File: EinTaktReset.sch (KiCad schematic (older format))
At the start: 22 parts

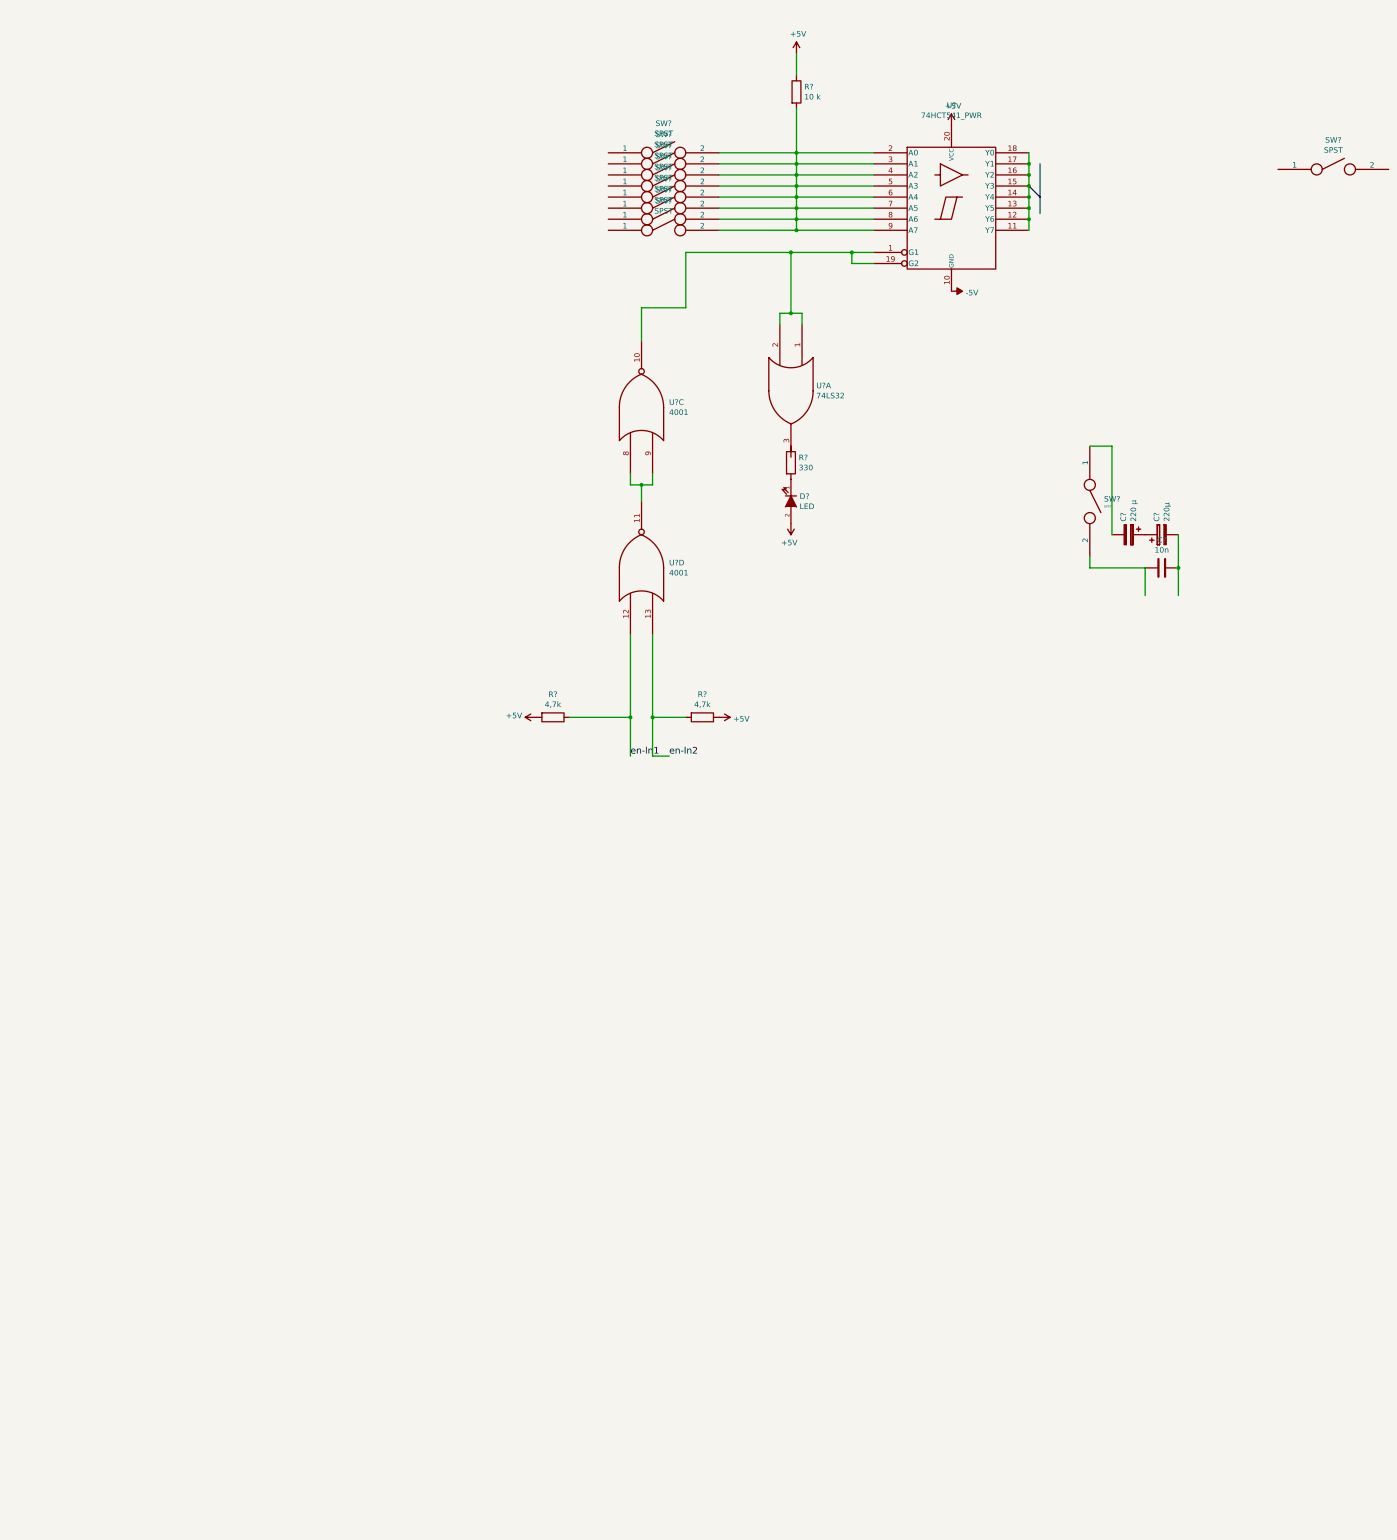
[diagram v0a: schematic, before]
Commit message: Schaltplan weitergeführt
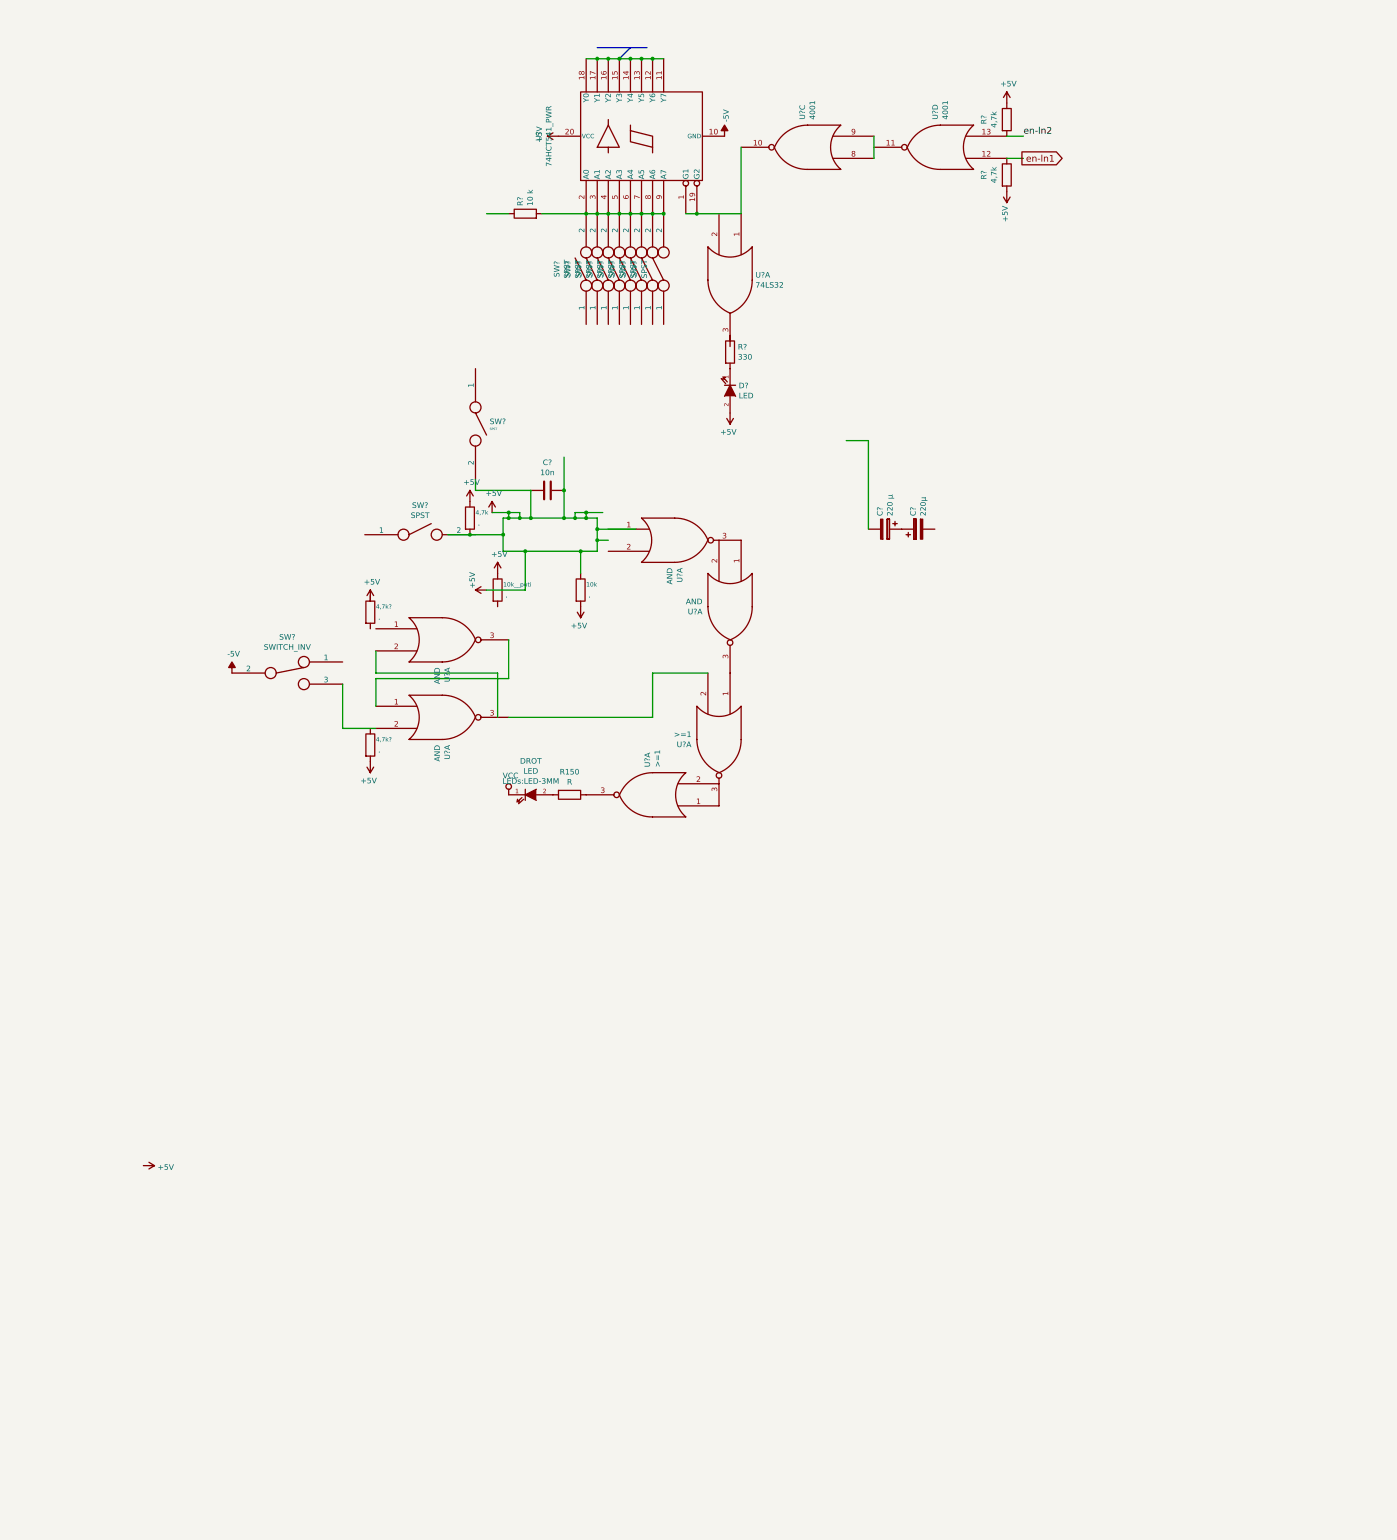
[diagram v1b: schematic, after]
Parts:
- removed SW?: SPST, symbol SPST
- added 10k, 10k__poti, 4,7k, 4,7k? (x2): ., symbol R
- added DROT: LED, LEDs:LED-3MM, symbol LED
- added R150: R, symbol R
- added SW?: SPST, symbol SPST
- added SW?: SWITCH_INV, symbol SWITCH_INV
- added U? (x4): AND, symbol 4001
- added U? (x2): >=1, symbol 4001
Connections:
- net labels added: VCC
- wire segments 36 -> 41
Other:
- moved on the sheet: C?, D?, R?, SW?, U?, U?A, U?C, U?D

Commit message: added lib
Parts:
- added IC?: 74LS624, symbol 74LS624
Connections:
- wire segments 41 -> 37
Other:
- moved on the sheet: 10k, 10k__poti, 4,7k, C?, SW?
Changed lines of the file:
@@
 LIBS:contrib
 LIBS:valves
+LIBS:vco
 LIBS:EinTaktReset-cache
 EELAYER 25 0
@@
 	0    1    1    0
 $EndComp
-Wire Wire Line
-	3100 5050 3100 4500
 $Comp
 L C C?
 U 1 1 57E97853
-P 2950 4800
-F 0 "C?" V 2698 4800 50  0000 C CNN
-F 1 "10n" V 2789 4800 50  0000 C CNN
-F 2 "" H 2988 4650 50  0000 C CNN
-F 3 "" H 2950 4800 50  0000 C CNN
-	1    2950 4800
-	0    1    1    0
-$EndComp
-Wire Wire Line
-	2800 4800 2300 4800
-Wire Wire Line
-	2300 4800 2300 4700
-Connection ~ 3100 4800
-Wire Wire Line
-	2800 5050 2800 4800
+P 2850 4100
+F 0 "C?" V 2598 4100 50  0000 C CNN
+F 1 "10n" V 2689 4100 50  0000 C CNN
+F 2 "" H 2888 3950 50  0000 C CNN
+F 3 "" H 2850 4100 50  0000 C CNN
+	1    2850 4100
+	0    1    1    0
+$EndComp
+Wire Wire Line
+	2200 4100 2200 4000
 $Comp
 L SPST SW?
 U 1 1 57E97A95
-P 2300 4200
-F 0 "SW?" V 2278 4328 50  0000 L CNN
-F 1 "SPST" V 2345 4328 20  0000 L CNN
-F 2 "" H 2300 4200 50  0000 C CNN
-F 3 "" H 2300 4200 50  0000 C CNN
-	1    2300 4200
+P 2200 3500
+F 0 "SW?" V 2178 3628 50  0000 L CNN
+F 1 "SPST" V 2245 3628 20  0000 L CNN
+F 2 "" H 2200 3500 50  0000 C CNN
+F 3 "" H 2200 3500 50  0000 C CNN
+	1    2200 3500
 	0    1    1    0
 $EndComp
@@
 	5850 4350 5850 5150
 Wire Wire Line
-	2550 5050 3400 5050
-Wire Wire Line
-	3400 5050 3400 5350
-Connection ~ 3100 5050
-Wire Wire Line
-	3400 5350 2550 5350
-Wire Wire Line
-	2550 5350 2550 5050
-Connection ~ 2800 5050
-Wire Wire Line
-	2700 5000 2700 5050
-Wire Wire Line
-	2450 5000 2700 5000
-Connection ~ 2700 5050
-Wire Wire Line
-	2600 5050 2600 5000
-Connection ~ 2600 5000
-Connection ~ 2600 5050
-Wire Wire Line
-	3200 5050 3200 5000
-Wire Wire Line
-	3200 5000 3450 5000
-Connection ~ 3200 5050
-Wire Wire Line
-	3300 5000 3300 5050
-Connection ~ 3300 5050
-Connection ~ 3300 5000
-Wire Wire Line
-	3400 5150 3750 5150
-Connection ~ 3400 5150
-Wire Wire Line
-	3400 5250 3500 5250
-Connection ~ 3400 5250
-Wire Wire Line
-	3250 5350 3250 5550
-Connection ~ 3250 5350
-Wire Wire Line
-	2750 5350 2750 5700
-Connection ~ 2750 5350
-Wire Wire Line
-	2050 5200 2550 5200
-Connection ~ 2550 5200
+	2300 4600 2550 4600
+Wire Wire Line
+	1350 5100 2050 5100
 $Comp
 L R 4,7k
 U 1 1 5845B97A
-P 2250 5050
-F 0 "4,7k" H 2300 5100 39  0000 L CNN
-F 1 "." H 2320 5005 50  0000 L CNN
-F 2 "" V 2180 5050 50  0000 C CNN
-F 3 "" H 2250 5050 50  0000 C CNN
-	1    2250 5050
-	1    0    0    -1
-$EndComp
-Connection ~ 2250 5200
+P 1550 4950
+F 0 "4,7k" H 1600 5000 39  0000 L CNN
+F 1 "." H 1620 4905 50  0000 L CNN
+F 2 "" V 1480 4950 50  0000 C CNN
+F 3 "" H 1550 4950 50  0000 C CNN
+	1    1550 4950
+	1    0    0    -1
+$EndComp
+Connection ~ 1550 5100
 $Comp
 L SPST SW?
 U 1 1 5845BEEF
-P 1800 5200
-F 0 "SW?" H 1800 5465 50  0000 C CNN
-F 1 "SPST" H 1800 5374 50  0000 C CNN
-F 2 "" H 1800 5200 50  0000 C CNN
-F 3 "" H 1800 5200 50  0000 C CNN
-	1    1800 5200
+P 1100 5100
+F 0 "SW?" H 1100 5365 50  0000 C CNN
+F 1 "SPST" H 1100 5274 50  0000 C CNN
+F 2 "" H 1100 5100 50  0000 C CNN
+F 3 "" H 1100 5100 50  0000 C CNN
+	1    1100 5100
 	1    0    0    -1
 $EndComp
@@
 L R 10k
 U 1 1 5845CFFB
-P 3250 5700
-F 0 "10k" H 3300 5750 39  0000 L CNN
-F 1 "." H 3320 5655 50  0000 L CNN
-F 2 "" V 3180 5700 50  0000 C CNN
-F 3 "" H 3250 5700 50  0000 C CNN
-	1    3250 5700
+P 2900 5850
+F 0 "10k" H 2950 5900 39  0000 L CNN
+F 1 "." H 2970 5805 50  0000 L CNN
+F 2 "" V 2830 5850 50  0000 C CNN
+F 3 "" H 2900 5850 50  0000 C CNN
+	1    2900 5850
 	1    0    0    -1
 $EndComp
@@
 L R 10k__poti
 U 1 1 5845D124
-P 2500 5700
-F 0 "10k__poti" H 2550 5750 39  0000 L CNN
-F 1 "." H 2570 5655 50  0000 L CNN
-F 2 "" V 2430 5700 50  0000 C CNN
-F 3 "" H 2500 5700 50  0000 C CNN
-	1    2500 5700
-	1    0    0    -1
-$EndComp
-Wire Wire Line
-	2750 5700 2400 5700
+P 2200 5700
+F 0 "10k__poti" H 2250 5750 39  0000 L CNN
+F 1 "." H 2270 5655 50  0000 L CNN
+F 2 "" V 2130 5700 50  0000 C CNN
+F 3 "" H 2200 5700 50  0000 C CNN
+	1    2200 5700
+	1    0    0    -1
+$EndComp
+Wire Wire Line
+	2450 5700 2100 5700
 $Comp
 L +5V #PWR?
 U 1 1 5845D52B
-P 2400 5700
-F 0 "#PWR?" H 2400 5550 50  0001 C CNN
-F 1 "+5V" H 2415 5828 0   0000 L CNN
-F 2 "" H 2400 5700 50  0000 C CNN
-F 3 "" H 2400 5700 50  0000 C CNN
-	1    2400 5700
+P 2100 5700
+F 0 "#PWR?" H 2100 5550 50  0001 C CNN
+F 1 "+5V" H 2115 5828 60  0000 L CNN
+F 2 "" H 2100 5700 50  0000 C CNN
+F 3 "" H 2100 5700 50  0000 C CNN
+	1    2100 5700
 	0    -1   -1   0
 $EndComp
@@
 L +5V #PWR?
 U 1 1 5845DB56
-P 2500 5550
-F 0 "#PWR?" H 2500 5400 50  0001 C CNN
-F 1 "+5V" H 2515 5723 50  0000 C CNN
-F 2 "" H 2500 5550 50  0000 C CNN
-F 3 "" H 2500 5550 50  0000 C CNN
-	1    2500 5550
+P 2200 5550
+F 0 "#PWR?" H 2200 5400 50  0001 C CNN
+F 1 "+5V" H 2215 5723 50  0000 C CNN
+F 2 "" H 2200 5550 50  0000 C CNN
+F 3 "" H 2200 5550 50  0000 C CNN
+	1    2200 5550
 	1    0    0    -1
 $EndComp
@@
 L +5V #PWR?
 U 1 1 5845DBA0
-P 2250 4900
-F 0 "#PWR?" H 2250 4750 50  0001 C CNN
-F 1 "+5V" H 2265 5073 50  0000 C CNN
-F 2 "" H 2250 4900 50  0000 C CNN
-F 3 "" H 2250 4900 50  0000 C CNN
-	1    2250 4900
+P 1550 4800
+F 0 "#PWR?" H 1550 4650 50  0001 C CNN
+F 1 "+5V" H 1565 4973 50  0000 C CNN
+F 2 "" H 1550 4800 50  0000 C CNN
+F 3 "" H 1550 4800 50  0000 C CNN
+	1    1550 4800
 	1    0    0    -1
 $EndComp
@@
 L +5V #PWR?
 U 1 1 5845DBEA
-P 2450 5000
-F 0 "#PWR?" H 2450 4850 50  0001 C CNN
-F 1 "+5V" H 2465 5173 50  0000 C CNN
-F 2 "" H 2450 5000 50  0000 C CNN
-F 3 "" H 2450 5000 50  0000 C CNN
-	1    2450 5000
+P 2300 4600
+F 0 "#PWR?" H 2300 4450 50  0001 C CNN
+F 1 "+5V" H 2315 4773 50  0000 C CNN
+F 2 "" H 2300 4600 50  0000 C CNN
+F 3 "" H 2300 4600 50  0000 C CNN
+	1    2300 4600
 	1    0    0    -1
 $EndComp
@@
 L +5V #PWR?
 U 1 1 5845DC34
-P 3250 5850
-F 0 "#PWR?" H 3250 5700 50  0001 C CNN
-F 1 "+5V" H 3265 6023 50  0000 C CNN
-F 2 "" H 3250 5850 50  0000 C CNN
-F 3 "" H 3250 5850 50  0000 C CNN
-	1    3250 5850
+P 2900 6000
+F 0 "#PWR?" H 2900 5850 50  0001 C CNN
+F 1 "+5V" H 2915 6173 50  0000 C CNN
+F 2 "" H 2900 6000 50  0000 C CNN
+F 3 "" H 2900 6000 50  0000 C CNN
+	1    2900 6000
 	-1   0    0    1
 $EndComp
@@
 Text GLabel 7600 1800 0    60   Input ~ 0
 en-ln1
+$Comp
+L 74LS624 IC?
+U 1 1 5A158E16
+P 2700 5100
+F 0 "IC?" H 2650 5200 60  0000 C CNN
+F 1 "74LS624" H 2700 5100 60  0000 C CNN
+F 2 "" H 2700 5100 60  0001 C CNN
+F 3 "" H 2700 5100 60  0001 C CNN
+	1    2700 5100
+	1    0    0    -1
+$EndComp
+Wire Wire Line
+	2700 4100 2700 4600
+Connection ~ 3000 4100
+Wire Wire Line
+	2700 4100 2200 4100
+Wire Wire Line
+	3000 4350 3000 3800
+Wire Wire Line
+	3000 4350 2800 4350
+Wire Wire Line
+	2800 4350 2800 4600
+Wire Wire Line
+	3350 4950 3450 4950
+Wire Wire Line
+	3450 4950 3450 5150
+Wire Wire Line
+	3450 5150 3500 5150
+Wire Wire Line
+	2900 4600 3200 4600
+Wire Wire Line
+	3200 4600 3200 4650
+Wire Wire Line
+	2450 5700 2450 5550
+Wire Wire Line
+	2900 5550 2900 5700
 $EndSCHEMATC

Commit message: .sch datei leicht verändert
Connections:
- net labels added: GND
- net labels removed: -5V
- wire segments 37 -> 43
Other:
- moved on the sheet: R?, SW?

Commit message: changes in eintaktreset .sch
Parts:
- added P? (x2): CONN_02X10, symbol CONN_02X10
- added U?: 74540, symbol 74540
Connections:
- wire segments 43 -> 46
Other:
- moved on the sheet: 10k, 10k__poti, 4,7k, 4,7k?, C?, D?, DROT, IC?, R150, R?, SW?, U?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

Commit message: changes in eintaktres .sch
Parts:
- added 10k? (x2): ., symbol R
- added C?: 10 µ, symbol CP
- added C?: 47µ, symbol CP
- added R?: 100, symbol R
- added SW?: SPST, symbol SPST
- added U? (x2): 74540, symbol 74540
- added U? (x2): AND, symbol 4001
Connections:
- wire segments 46 -> 67
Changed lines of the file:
@@
 	1    0    0    -1
-$EndComp
-$Comp
-L +5V #PWR?
-U 1 1 57E966CE
-P -650 11250
-F 0 "#PWR?" H -650 11100 50  0001 C CNN
-F 1 "+5V" V -635 11378 50  0000 L CNN
-F 2 "" H -650 11250 50  0000 C CNN
-F 3 "" H -650 11250 50  0000 C CNN
-	1    -650 11250
-	0    1    1    0
 $EndComp
 Text Label 7400 1950 0    60   ~ 0
@@
 	0    -1   -1   0
 $EndComp
+$Comp
+L 74540 U?
+U 1 1 5A31340A
+P 1450 9150
+F 0 "U?" H 1550 9250 60  0000 C CNN
+F 1 "74540" H 1600 9000 60  0000 C CNN
+F 2 "" H 1600 9000 60  0001 C CNN
+F 3 "" H 1600 9000 60  0001 C CNN
+	1    1450 9150
+	0    -1   -1   0
+$EndComp
+$Comp
+L 74540 U?
+U 1 1 5A313566
+P 1450 10000
+F 0 "U?" H 1550 10100 60  0000 C CNN
+F 1 "74540" H 1600 9850 60  0000 C CNN
+F 2 "" H 1600 9850 60  0001 C CNN
+F 3 "" H 1600 9850 60  0001 C CNN
+	1    1450 10000
+	0    -1   -1   0
+$EndComp
+Wire Wire Line
+	1450 9600 1450 9500
+Wire Wire Line
+	1450 8750 1450 8650
+Wire Wire Line
+	1450 10350 1450 10500
+Wire Wire Line
+	1450 10500 950  10500
+$Comp
+L R 10k?
+U 1 1 5A314363
+P 950 10300
+F 0 "10k?" H 1000 10350 39  0000 L CNN
+F 1 "." H 1020 10255 50  0000 L CNN
+F 2 "" V 880 10300 50  0000 C CNN
+F 3 "" H 950 10300 50  0000 C CNN
+	1    950  10300
+	1    0    0    -1
+$EndComp
+$Comp
+L +5V #PWR?
+U 1 1 5A314781
+P 950 10150
+F 0 "#PWR?" H 950 10000 50  0001 C CNN
+F 1 "+5V" H 965 10323 50  0000 C CNN
+F 2 "" H 950 10150 50  0000 C CNN
+F 3 "" H 950 10150 50  0000 C CNN
+	1    950  10150
+	1    0    0    -1
+$EndComp
+Wire Wire Line
+	950  10450 950  10550
+Connection ~ 950  10500
+$Comp
+L CP C?
+U 1 1 5A315184
+P 950 10700
+F 0 "C?" H 975 10800 50  0000 L CNN
+F 1 "10 µ" H 975 10600 50  0000 L CNN
+F 2 "" H 988 10550 50  0000 C CNN
+F 3 "" H 950 10700 50  0000 C CNN
+	1    950  10700
+	1    0    0    -1
+$EndComp
+$Comp
+L GND #PWR?
+U 1 1 5A31526B
+P 950 10850
+F 0 "#PWR?" H 950 10600 50  0001 C CNN
+F 1 "GND" H 950 10700 50  0000 C CNN
+F 2 "" H 950 10850 50  0000 C CNN
+F 3 "" H 950 10850 50  0000 C CNN
+	1    950  10850
+	1    0    0    -1
+$EndComp
+Wire Wire Line
+	3550 5700 3300 5700
+Wire Wire Line
+	3300 5700 3300 7450
+Wire Wire Line
+	3300 7450 2350 7450
+Wire Wire Line
+	2350 7450 2350 12800
+Connection ~ 2350 8300
+Wire Wire Line
+	1450 8300 1800 8300
+Wire Wire Line
+	1800 8300 1800 10300
+Wire Wire Line
+	1800 10300 2350 10300
+Connection ~ 2350 10300
+Wire Wire Line
+	1450 10000 1800 10000
+Connection ~ 1800 10000
+Wire Wire Line
+	1450 9150 1800 9150
+Connection ~ 1800 9150
+$Comp
+L 4001 U?
+U 1 1 5A31755C
+P 1750 12800
+F 0 "U?" V 1796 12551 50  0000 R CNN
+F 1 "AND" V 1705 12551 50  0000 R CNN
+F 2 "" H 1750 12800 60  0001 C CNN
+F 3 "" H 1750 12800 60  0001 C CNN
+	1    1750 12800
+	1    0    0    -1
+$EndComp
+$Comp
+L 4001 U?
+U 1 1 5A317BD1
+P 300 12800
+F 0 "U?" V 346 12551 50  0000 R CNN
+F 1 "AND" V 255 12551 50  0000 R CNN
+F 2 "" H 300 12800 60  0001 C CNN
+F 3 "" H 300 12800 60  0001 C CNN
+	1    300  12800
+	1    0    0    -1
+$EndComp
+Wire Wire Line
+	900  12800 1150 12800
+Wire Wire Line
+	1150 12700 1150 12900
+Connection ~ 1150 12800
+Wire Wire Line
+	-300 12900 -300 12700
+Wire Wire Line
+	-1600 12800 -300 12800
+Connection ~ -300 12800
+$Comp
+L +5V #PWR?
+U 1 1 57E966CE
+P -1500 12050
+F 0 "#PWR?" H -1500 11900 50  0001 C CNN
+F 1 "+5V" V -1485 12178 50  0000 L CNN
+F 2 "" H -1500 12050 50  0000 C CNN
+F 3 "" H -1500 12050 50  0000 C CNN
+	1    -1500 12050
+	1    0    0    -1
+$EndComp
+$Comp
+L +5V #PWR?
+U 1 1 5A318CCB
+P -1100 12050
+F 0 "#PWR?" H -1100 11900 50  0001 C CNN
+F 1 "+5V" V -1085 12178 50  0000 L CNN
+F 2 "" H -1100 12050 50  0000 C CNN
+F 3 "" H -1100 12050 50  0000 C CNN
+	1    -1100 12050
+	1    0    0    -1
+$EndComp
+$Comp
+L R 10k?
+U 1 1 5A318D8E
+P -1500 12200
+F 0 "10k?" H -1450 12250 39  0000 L CNN
+F 1 "." H -1430 12155 50  0000 L CNN
+F 2 "" V -1570 12200 50  0000 C CNN
+F 3 "" H -1500 12200 50  0000 C CNN
+	1    -1500 12200
+	1    0    0    -1
+$EndComp
+$Comp
+L CP C?
+U 1 1 5A319373
+P -1100 13450
+F 0 "C?" H -1075 13550 50  0000 L CNN
+F 1 "47µ" H -1075 13350 50  0000 L CNN
+F 2 "" H -1062 13300 50  0000 C CNN
+F 3 "" H -1100 13450 50  0000 C CNN
+	1    -1100 13450
+	1    0    0    -1
+$EndComp
+$Comp
+L R R?
+U 1 1 5A31AE8F
+P -1100 13150
+F 0 "R?" H -1050 13200 39  0000 L CNN
+F 1 "100" H -1030 13105 50  0000 L CNN
+F 2 "" V -1170 13150 50  0000 C CNN
+F 3 "" H -1100 13150 50  0000 C CNN
+	1    -1100 13150
+	1    0    0    -1
+$EndComp
+$Comp
+L GND #PWR?
+U 1 1 5A31B31B
+P -1100 13600
+F 0 "#PWR?" H -1100 13350 50  0001 C CNN
+F 1 "GND" H -1100 13450 50  0000 C CNN
+F 2 "" H -1100 13600 50  0000 C CNN
+F 3 "" H -1100 13600 50  0000 C CNN
+	1    -1100 13600
+	1    0    0    -1
+$EndComp
+$Comp
+L SPST SW?
+U 1 1 5A31B889
+P -1600 13500
+F 0 "SW?" H -1600 13765 50  0000 C CNN
+F 1 "SPST" H -1600 13674 50  0000 C CNN
+F 2 "" H -1600 13500 50  0000 C CNN
+F 3 "" H -1600 13500 50  0000 C CNN
+	1    -1600 13500
+	0    -1   -1   0
+$EndComp
+$Comp
+L GND #PWR?
+U 1 1 5A31BD75
+P -1600 14000
+F 0 "#PWR?" H -1600 13750 50  0001 C CNN
+F 1 "GND" H -1600 13850 50  0000 C CNN
+F 2 "" H -1600 14000 50  0000 C CNN
+F 3 "" H -1600 14000 50  0000 C CNN
+	1    -1600 14000
+	1    0    0    -1
+$EndComp
+Wire Wire Line
+	-1600 12800 -1600 13000
+Wire Wire Line
+	-1100 13000 -1100 12800
+Connection ~ -1100 12800
+Wire Wire Line
+	-1500 12350 -1500 12800
+Connection ~ -1500 12800
 $EndSCHEMATC

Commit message: reset logic added
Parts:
- added D?: D, symbol D
- added R? (x2): 470, symbol R
- added R? (x2): 2,2k, symbol R
- added R? (x2): 1,8k, symbol R
- added SW?: SWITCH_INV, symbol SWITCH_INV
- added U?: >=1, symbol 4001
- added U? (x5): 74540, symbol 74540
- D?, DROT: symbol LED -> LED-RESCUE-EinTaktReset
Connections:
- wire segments 67 -> 112
